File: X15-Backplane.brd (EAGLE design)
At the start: 139.7 x 100 mm, 34 parts, among them U1 ULN2003AD

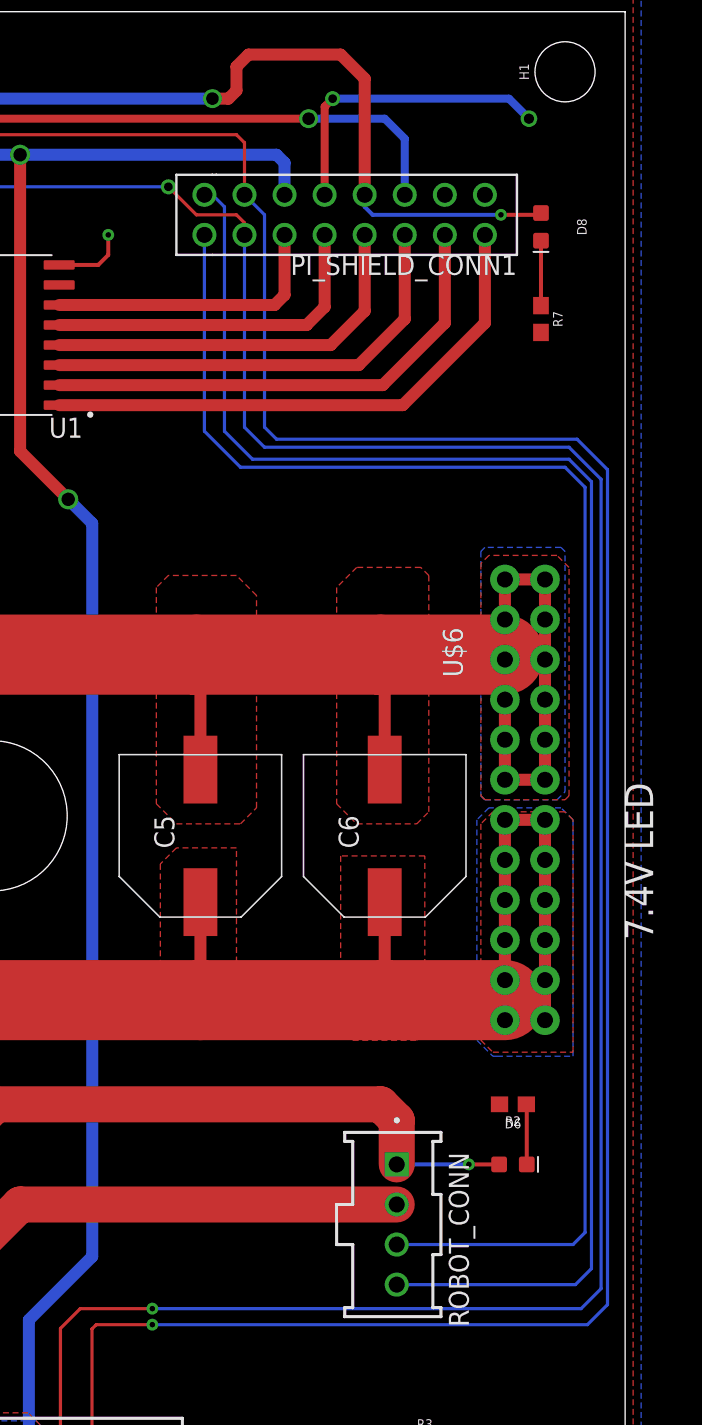
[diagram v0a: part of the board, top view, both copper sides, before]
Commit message: fixed dimensions
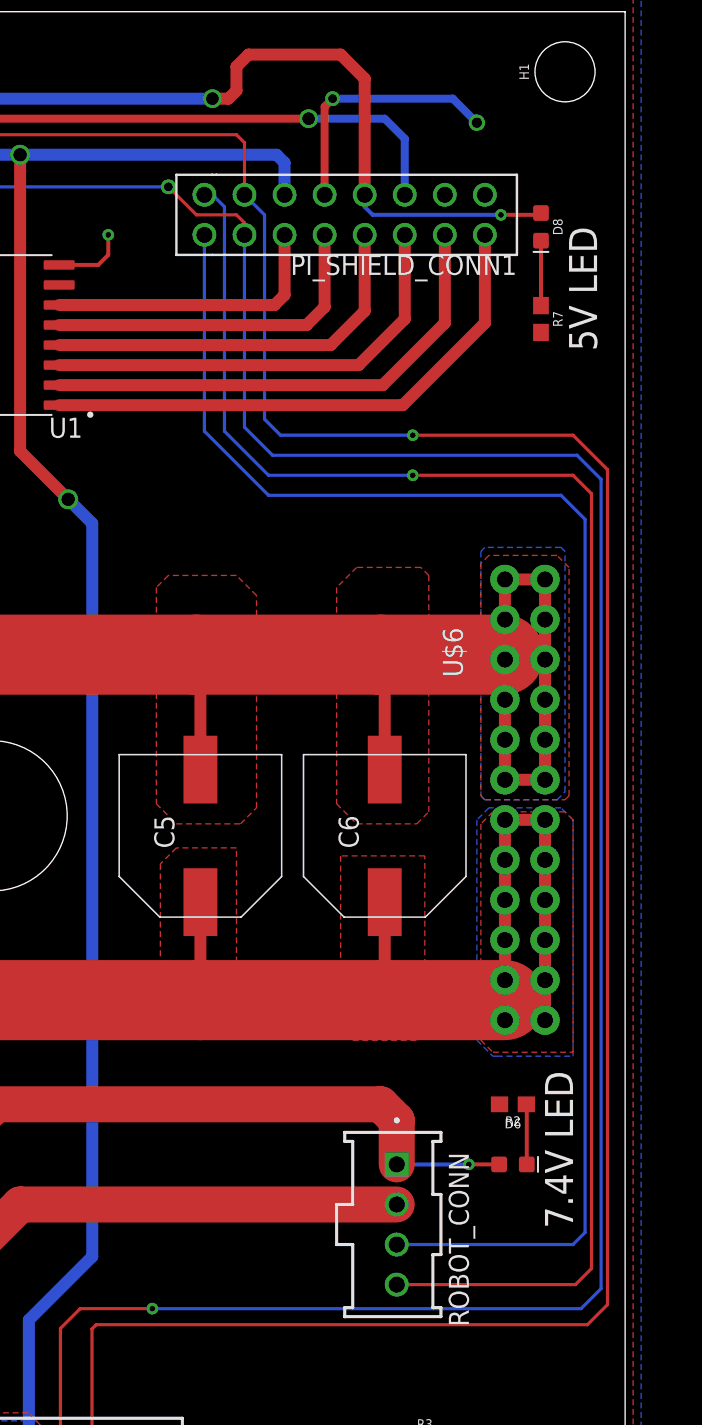
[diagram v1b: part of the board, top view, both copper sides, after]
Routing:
- net GND: track 50.7 -> 47.5 mm
- net ROBOT_ARM: track 97.5 -> 96.4 mm
- net ROBOT_ARM_2: track 103.1 -> 102.6 mm, vias 0 -> 1
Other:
- board text added: "5V LED"
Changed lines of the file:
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@@
 Rachel Livesay
 Hyunseok Hong</text>
-<text x="141.478" y="41.148" size="1.778" layer="25" rot="R90">7.4V LED</text>
+<text x="136.398" y="22.86" size="1.778" layer="25" rot="R90">7.4V LED</text>
 <text x="52.324" y="41.148" size="1.778" layer="25">12V LED</text>
+<text x="137.922" y="78.486" size="1.778" layer="25" rot="R90">5V LED</text>
 </plain>
 <attributes>
@@
 </element>
 <element name="D8" library="SparkFun-LED" library_urn="urn:adsk.eagle:library:529" package="LED-0603" package3d_urn="urn:adsk.eagle:package:39354/1" value="" x="134.366" y="86.36" smashed="yes" rot="R270">
-<attribute name="NAME" x="136.652" y="86.36" size="0.6096" layer="25" font="vector" ratio="20" rot="R270" align="bottom-center"/>
+<attribute name="NAME" x="135.128" y="86.36" size="0.6096" layer="25" font="vector" ratio="20" rot="R270" align="bottom-center"/>
 <attribute name="VALUE" x="132.08" y="86.36" size="0.6096" layer="27" font="vector" ratio="20" rot="R270" align="top-center"/>
 </element>
@@
 <wire x1="115.57" y1="86.614" x2="115.57" y2="85.852" width="0.2032" layer="1"/>
 <wire x1="115.57" y1="85.852" x2="115.57" y2="73.66" width="0.2032" layer="16"/>
-<wire x1="115.57" y1="73.66" x2="116.84" y2="72.39" width="0.2032" layer="16"/>
-<wire x1="116.84" y1="72.39" x2="136.144" y2="72.39" width="0.2032" layer="16"/>
-<wire x1="136.144" y1="72.39" x2="138.176" y2="70.358" width="0.2032" layer="16"/>
+<wire x1="115.57" y1="73.66" x2="117.348" y2="71.882" width="0.2032" layer="16"/>
+<wire x1="117.348" y1="71.882" x2="136.652" y2="71.882" width="0.2032" layer="16"/>
+<wire x1="136.652" y1="71.882" x2="138.176" y2="70.358" width="0.2032" layer="16"/>
 <wire x1="138.176" y1="70.358" x2="138.176" y2="19.05" width="0.2032" layer="16"/>
 <wire x1="138.176" y1="19.05" x2="136.906" y2="17.78" width="0.2032" layer="16"/>
@@
 <wire x1="105.902" y1="9.382" x2="105.902" y2="16.494" width="0.2032" layer="1"/>
 <wire x1="105.902" y1="16.494" x2="106.172" y2="16.764" width="0.2032" layer="1"/>
-<wire x1="106.172" y1="16.764" x2="109.728" y2="16.764" width="0.2032" layer="1"/>
-<via x="109.728" y="16.764" extent="1-16" drill="0.35"/>
 <wire x1="18.417" y1="81.354" x2="17.793" y2="81.978" width="0.2032" layer="1"/>
 <wire x1="17.793" y1="81.978" x2="16.777" y2="81.978" width="0.2032" layer="1"/>
@@
 <wire x1="115.57" y1="91.694" x2="115.062" y2="92.202" width="0.2032" layer="1"/>
 <wire x1="115.57" y1="88.392" x2="116.84" y2="87.122" width="0.2032" layer="16"/>
-<wire x1="116.84" y1="87.122" x2="116.84" y2="73.66" width="0.2032" layer="16"/>
-<wire x1="116.84" y1="73.66" x2="117.602" y2="72.898" width="0.2032" layer="16"/>
-<wire x1="117.602" y1="72.898" x2="136.652" y2="72.898" width="0.2032" layer="16"/>
-<wire x1="136.652" y1="72.898" x2="138.5824" y2="70.9676" width="0.2032" layer="16"/>
-<wire x1="138.5824" y1="70.9676" x2="138.5824" y2="18.034" width="0.2032" layer="16"/>
-<wire x1="138.5824" y1="18.034" x2="137.3124" y2="16.764" width="0.2032" layer="16"/>
-<wire x1="137.3124" y1="16.764" x2="109.728" y2="16.764" width="0.2032" layer="16"/>
+<wire x1="116.84" y1="87.122" x2="116.84" y2="74.168" width="0.2032" layer="16"/>
+<wire x1="116.84" y1="74.168" x2="117.856" y2="73.152" width="0.2032" layer="16"/>
+<wire x1="126.238" y1="73.152" x2="117.856" y2="73.152" width="0.2032" layer="16"/>
+<wire x1="136.398" y1="73.152" x2="126.238" y2="73.152" width="0.2032" layer="1"/>
+<wire x1="136.398" y1="73.152" x2="138.5824" y2="70.9676" width="0.2032" layer="1"/>
+<wire x1="138.5824" y1="70.9676" x2="138.5824" y2="18.034" width="0.2032" layer="1"/>
+<wire x1="138.5824" y1="18.034" x2="137.3124" y2="16.764" width="0.2032" layer="1"/>
+<wire x1="137.3124" y1="16.764" x2="106.172" y2="16.764" width="0.2032" layer="1"/>
+<via x="126.238" y="73.152" extent="1-16" drill="0.35"/>
 </signal>
 <signal name="12V">
@@
 <contactref element="R1" pad="2"/>
 <contactref element="U1" pad="8"/>
-<via x="133.604" y="93.218" extent="1-16" drill="0.65"/>
+<via x="130.302" y="92.964" extent="1-16" drill="0.65"/>
 <wire x1="56.388" y1="98.044" x2="65.786" y2="98.044" width="0.508" layer="16"/>
 <wire x1="65.786" y1="98.044" x2="68.072" y2="95.758" width="0.508" layer="16"/>
@@
 <via x="121.158" y="94.488" extent="1-16" drill="0.55"/>
 <wire x1="120.65" y1="88.392" x2="120.65" y2="93.98" width="0.508" layer="1"/>
-<wire x1="121.158" y1="94.488" x2="132.334" y2="94.488" width="0.508" layer="16"/>
-<wire x1="132.334" y1="94.488" x2="133.604" y2="93.218" width="0.508" layer="16"/>
+<wire x1="121.158" y1="94.488" x2="128.778" y2="94.488" width="0.508" layer="16"/>
+<wire x1="128.778" y1="94.488" x2="130.302" y2="92.964" width="0.508" layer="16"/>
 <via x="106.934" y="85.852" extent="1-16" drill="0.35"/>
 <wire x1="103.821" y1="83.947" x2="106.299" y2="83.947" width="0.254" layer="1"/>
@@
 <contactref element="ROBOT_CONN" pad="03"/>
 <wire x1="113.03" y1="85.852" x2="113.03" y2="73.406" width="0.2032" layer="16"/>
-<wire x1="113.03" y1="73.406" x2="115.316" y2="71.12" width="0.2032" layer="16"/>
-<wire x1="115.316" y1="71.12" x2="135.89" y2="71.12" width="0.2032" layer="16"/>
-<wire x1="135.89" y1="71.12" x2="137.16" y2="69.85" width="0.2032" layer="16"/>
-<wire x1="137.16" y1="69.85" x2="137.16" y2="22.606" width="0.2032" layer="16"/>
+<wire x1="113.03" y1="73.406" x2="117.094" y2="69.342" width="0.2032" layer="16"/>
+<wire x1="117.094" y1="69.342" x2="135.636" y2="69.342" width="0.2032" layer="16"/>
+<wire x1="135.636" y1="69.342" x2="137.16" y2="67.818" width="0.2032" layer="16"/>
+<wire x1="137.16" y1="67.818" x2="137.16" y2="22.606" width="0.2032" layer="16"/>
 <wire x1="137.16" y1="22.606" x2="136.398" y2="21.844" width="0.2032" layer="16"/>
 <wire x1="136.398" y1="21.844" x2="125.222" y2="21.844" width="0.2032" layer="16"/>
@@
 <wire x1="114.3" y1="87.63" x2="114.3" y2="73.406" width="0.2032" layer="16"/>
 <wire x1="113.538" y1="88.392" x2="114.3" y2="87.63" width="0.2032" layer="16"/>
-<wire x1="114.3" y1="73.406" x2="116.078" y2="71.628" width="0.2032" layer="16"/>
-<wire x1="116.078" y1="71.628" x2="136.144" y2="71.628" width="0.2032" layer="16"/>
-<wire x1="136.144" y1="71.628" x2="137.5664" y2="70.2056" width="0.2032" layer="16"/>
-<wire x1="137.5664" y1="70.2056" x2="137.5664" y2="20.32" width="0.2032" layer="16"/>
-<wire x1="137.5664" y1="20.32" x2="136.5504" y2="19.304" width="0.2032" layer="16"/>
-<wire x1="136.5504" y1="19.304" x2="125.222" y2="19.304" width="0.2032" layer="16"/>
+<wire x1="114.3" y1="73.406" x2="117.094" y2="70.612" width="0.2032" layer="16"/>
+<wire x1="126.238" y1="70.612" x2="117.094" y2="70.612" width="0.2032" layer="16"/>
+<wire x1="136.398" y1="70.612" x2="126.238" y2="70.612" width="0.2032" layer="1"/>
+<wire x1="136.398" y1="70.612" x2="137.5664" y2="69.4436" width="0.2032" layer="1"/>
+<wire x1="137.5664" y1="69.4436" x2="137.5664" y2="20.32" width="0.2032" layer="1"/>
+<wire x1="137.5664" y1="20.32" x2="136.5504" y2="19.304" width="0.2032" layer="1"/>
+<wire x1="136.5504" y1="19.304" x2="125.222" y2="19.304" width="0.2032" layer="1"/>
+<via x="126.238" y="70.612" extent="1-16" drill="0.35"/>
 </signal>
 </signals>
